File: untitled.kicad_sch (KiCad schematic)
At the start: 4 parts, among them Y1 Crystal_GND24

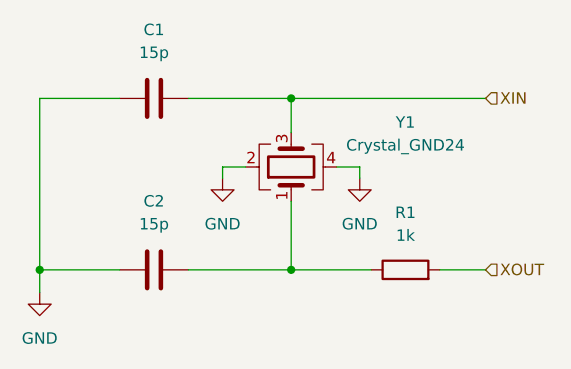
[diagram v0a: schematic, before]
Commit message: Complete schematic for first prototype
- Footprints: passives 0402/0603 (larger only for 24 V / DC bias),
  U1 and L1 footprints taken from RP2350A Minimal R4 reference (MIT)
- New sheet vystupy: heater (Q1 SiS434DN) with thermal fuse terminal J13,
  fan (GPIO13) and exhaust fan (GPIO12) with AO3422, input protection
  (fuse, AOD4185 reverse polarity, SMBJ24CA TVS, bulk cap), status LED on
  RM2 GPIO0, button GPIO15, NTC on ADC0 (22k pull-up), I2C1 pull-ups,
  second SHT40 on I2C0 (GPIO8/9)
- New sheet rozsireni: spare GPIO header J12, test points TP1-TP5,
  mounting holes H1-H4
- Selected parts with Manufacturer/MPN fields; L2 4.7 uH Wurth 74438356047
- Fix D2 pin mapping (Device:D_Schottky), remove duplicate pull-down R12,
  C16 changed to 100 nF for third DVDD pin, Y1 value set
- Project footprint library susicka.pretty (PowerPAK 1212-8 with G/S/D pads)

Co-Authored-By: Claude Opus 5.5 <noreply@anthropic.com>
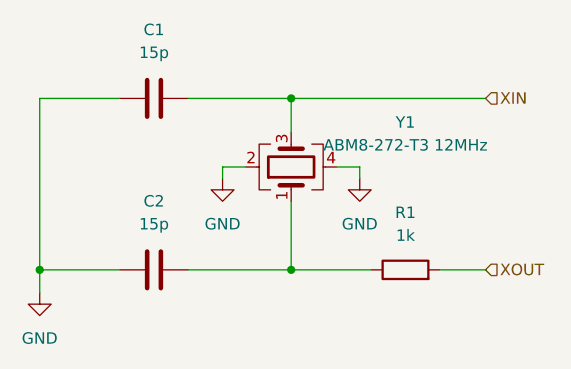
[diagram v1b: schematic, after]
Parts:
- C1, C2: footprint Capacitor_SMD:C_0603_1608Metric -> Capacitor_SMD:C_0402_1005Metric
- Y1: value Crystal_GND24 -> ABM8-272-T3 12MHz
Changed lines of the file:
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@@
 			)
 		)
-		(property "Footprint" "Capacitor_SMD:C_0603_1608Metric"
+		(property "Footprint" "Capacitor_SMD:C_0402_1005Metric"
 			(at 116.84 93.0148 0)
 			(effects
@@
 			)
 		)
-		(property "Value" "Crystal_GND24"
+		(property "Value" "ABM8-272-T3 12MHz"
 			(at 140.97 99.1868 90)
 			(effects
@@
 			)
 		)
-		(property "Footprint" "Capacitor_SMD:C_0603_1608Metric"
+		(property "Footprint" "Capacitor_SMD:C_0402_1005Metric"
 			(at 116.84 112.0648 0)
 			(effects
